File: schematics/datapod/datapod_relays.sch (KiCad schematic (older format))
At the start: 8 parts, among them K1 DS2E-SL2-DC5V, K2 DS2E-SL2-DC5V, Q1 FDG1024NZ, Q2 FDG1024NZ

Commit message: modified schematic
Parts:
- K1, K2: symbol Relays_user_made:DS2E-SL2-DC5V -> datapod-rescue:DS2E-SL2-DC5V-Relays_user_made
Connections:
- net +5V: now also K1.~, K2.~
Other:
- note added: "APPLIES +14.8V TO WIRE/PIN #3\nOF THE LPBH-MP CONNECTOR.\n\nWIRE/PIN #4 SHOULD BE \nCONNECTED TO GND \n\n"
- note added: "THE RELAYS ARE IN A RESET CONDITION WHEN THE\nCOIL ON PINS 2 & 15 IS ACTIVATED. iN A RESET CONDITION\n4 & 6 ARE SHORTED AND 13 &11 ARE SHORTED.\n\nWHEN THE COIL ON PINS 1 & 16 IS ACTIVATED THEN PINS 4 & 8 ARE\nSHORTED AND PINS 13 & 9 ARE SHORTED."
- note added: "THIS REALY WILL BE USED TO\nTURN ON THE RASPBERRY PI\nAND THE IRIDIUM MODEM."
- note added: "THIS RELAY WILL BE USED TO \nENABLE THE BURN WIRE RELEASE"
- moved on the sheet: D1, D2, D3, D4, Q1A, Q1B, Q2A, Q2B

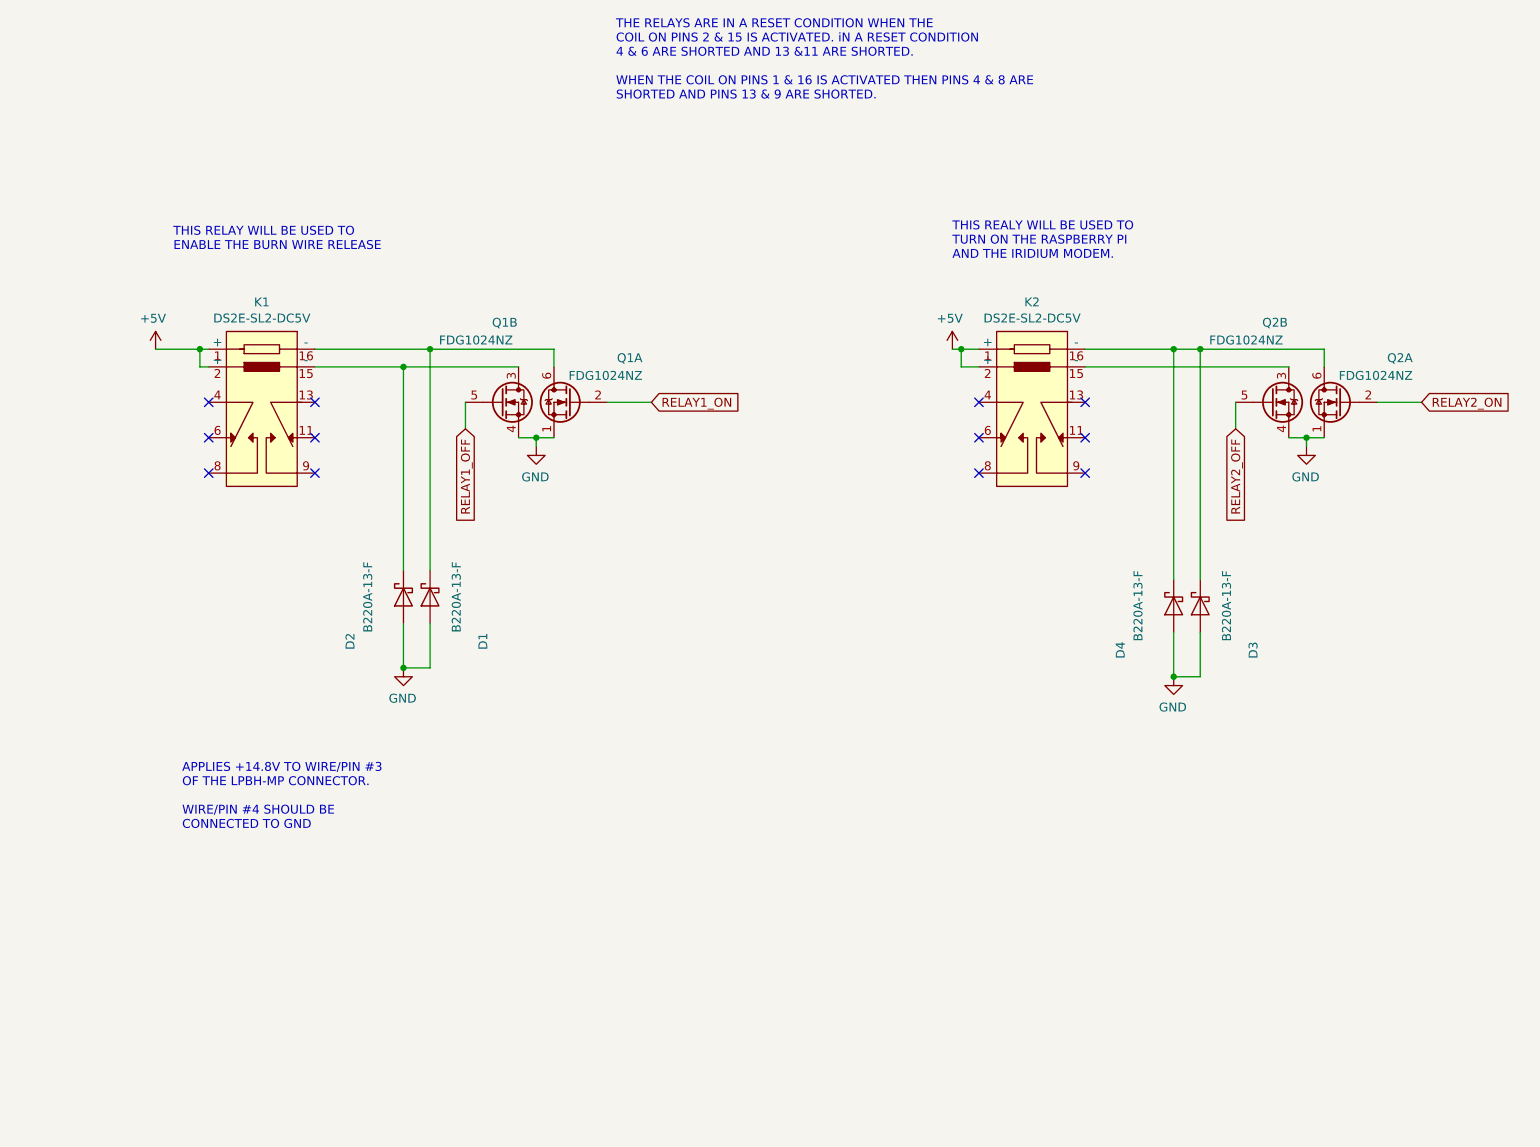
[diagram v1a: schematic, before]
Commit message: added more connectors and started drawing the PCB
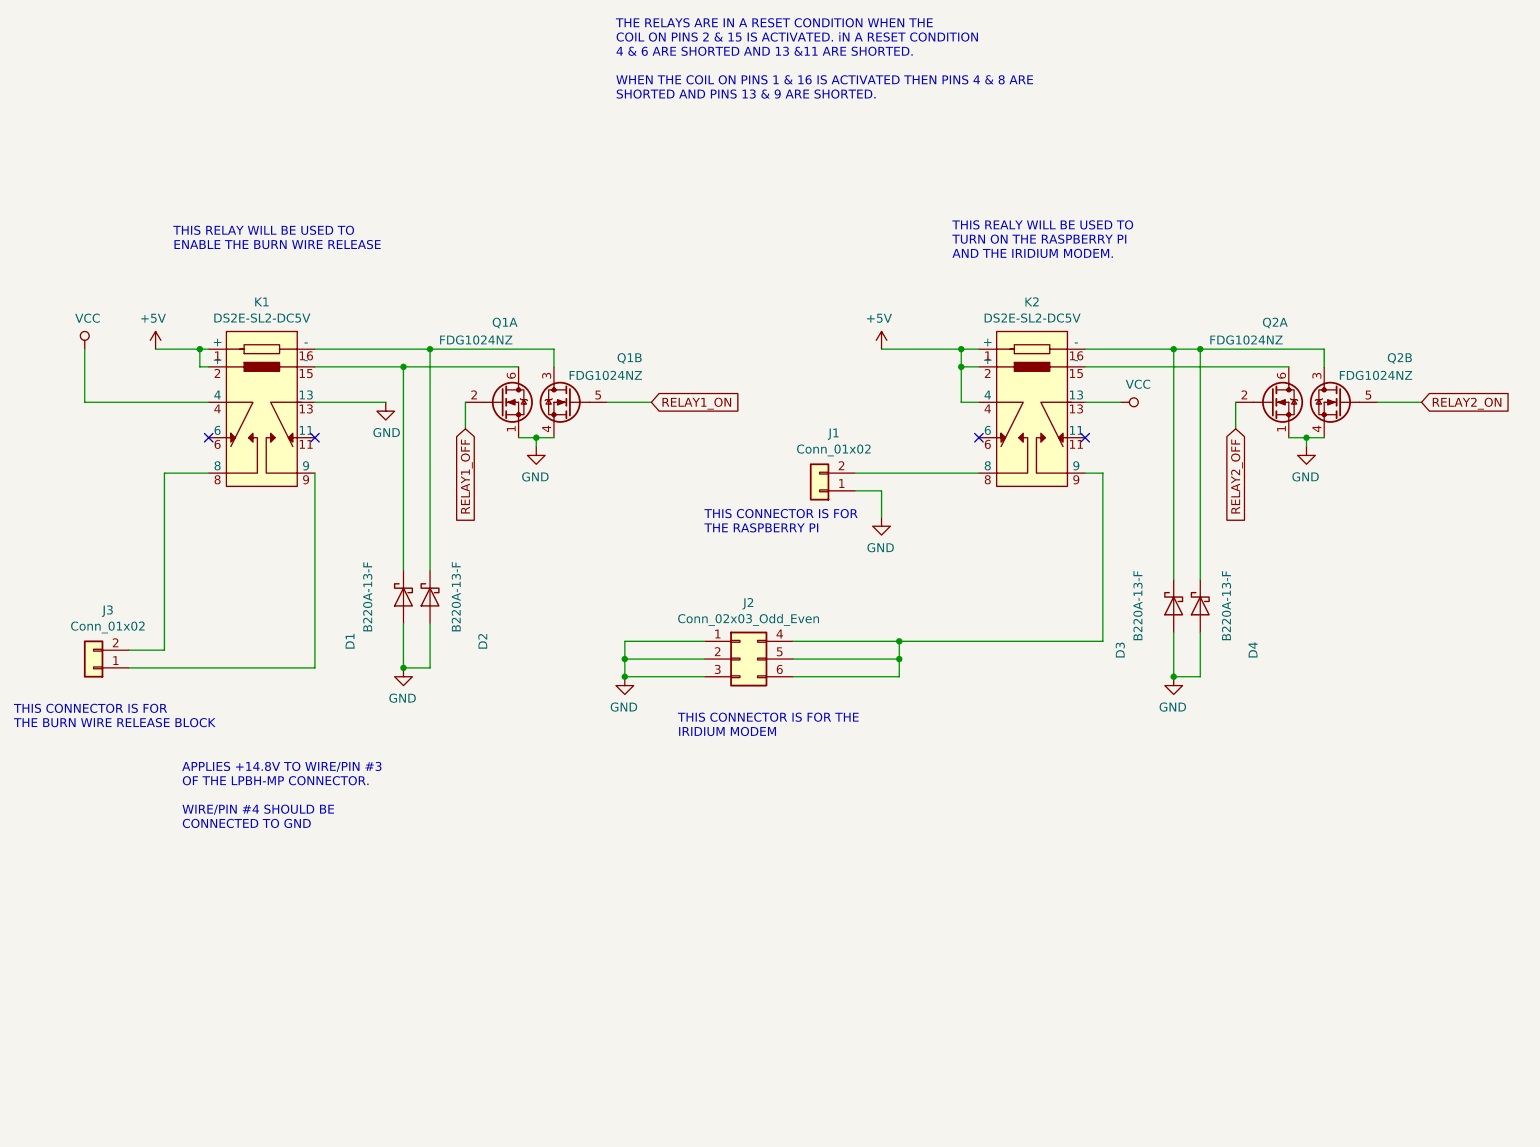
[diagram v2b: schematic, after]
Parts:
- removed K1, K2: DS2E-SL2-DC5V, Package_DIP:DIP-16_W7.62mm_SMDSocket_SmallPads, symbol datapod-rescue:DS2E-SL2-DC5V-Relays_user_made
- added J1: Conn_01x02, Connector_Molex:Molex_Mini-Fit_Jr_5569-02A1_2x01_P4.20mm_Horizontal, symbol Connector_Generic:Conn_01x02
- added J2: Conn_02x03_Odd_Even, Connector_Molex:Molex_Mega-Fit_76825-0006_2x03_P5.70mm_Horizontal, symbol Connector_Generic:Conn_02x03_Top_Bottom
- added J3: Conn_01x02, Connector_Molex:Molex_Mega-Fit_76825-0002_2x01_P5.70mm_Horizontal, symbol Connector_Generic:Conn_01x02
- added K1, K2: DS2E-SL2-DC5V, Package_DIP:DIP-16_W7.62mm_SMDSocket_SmallPads, symbol Relays_user_made:DS2E-SL2-DC5V
- renumbered D2 to D1, D1 to D2, D4 to D3, D3 to D4
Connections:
- net +5V: now also K1.1 (+), K1.2 (+), K2.1 (+), K2.2 (+), K2.4
- net GND: now also Q1.1 (S), Q1.4 (S), Q2.1 (S), Q2.4 (S), J1.1 (Pin_1), J2.1 (Pin_1), J2.2 (Pin_2), J2.3 (Pin_3), K1.13; no longer Q1.1 (S), Q1.4 (S), Q2.1 (S), Q2.4 (S)
- net RELAY1_OFF: now also Q1.2 (G); no longer Q1.5 (G)
- net RELAY1_ON: now also Q1.5 (G); no longer Q1.2 (G)
- net RELAY2_OFF: now also Q2.2 (G); no longer Q2.5 (G)
- net RELAY2_ON: now also Q2.5 (G); no longer Q2.2 (G)
- net at D3.1 (K), D4.1 (K): now also Q2.3 (D), K2.16 (-); no longer Q2.6 (D)
- net at D1.1 (K): now also Q1.6 (D), K1.15 (-); no longer Q1.3 (D)
- net at D2.1 (K): now also Q1.3 (D), K1.16 (-); no longer Q1.6 (D)
- new net: J3.1 (Pin_1), K1.9
- new net: J3.2 (Pin_2), K1.8
- new net: J2.4 (Pin_4), J2.5 (Pin_5), J2.6 (Pin_6), K2.9
- new net: K2.15 (-), Q2.6 (D)
- new net: J1.2 (Pin_2), K2.8
- new net VCC: K1.4, K2.13
- no-connect marks 12 -> 4
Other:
- note added: "THIS CONNECTOR IS FOR THE\nIRIDIUM MODEM"
- note added: "THIS CONNECTOR IS FOR \nTHE RASPBERRY PI"
- note added: "THIS CONNECTOR IS FOR\nTHE BURN WIRE RELEASE BLOCK"

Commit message: added final routed PCB, gerbers and BOM
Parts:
- D1, D2, D3, D4: Part# (none) -> B220A-FDIDKR-ND
- K1, K2: Part# (none) -> 255-1066-ND; Vendor (none) -> Digikey
- Q1, Q2: Part# (none) -> FDG1024NZFSCT-ND; part# FDG1024NZFSCT-ND -> (none)
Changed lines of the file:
@@
 F 3 "http://www.fairchildsemi.com/ds/FD/FDG1024NZ.pdf" H 3900 3000 50  0001 L CNN
 F 4 "Digikey" H 3900 3000 50  0001 C CNN "Vendor"
-F 5 "FDG1024NZFSCT-ND" H 3900 3000 50  0001 C CNN "part#"
+F 5 "FDG1024NZFSCT-ND" H 3900 3000 50  0001 C CNN "Part#"
 	2    3900 3000
 	-1   0    0    -1
@@
 F 3 "http://www.fairchildsemi.com/ds/FD/FDG1024NZ.pdf" H 3500 3000 50  0001 L CNN
 F 4 "Digikey" H 3500 3000 50  0001 C CNN "Vendor"
-F 5 "FDG1024NZFSCT-ND" H 3500 3000 50  0001 C CNN "part#"
+F 5 "FDG1024NZFSCT-ND" H 3500 3000 50  0001 C CNN "Part#"
 	1    3500 3000
 	1    0    0    -1
@@
 F 3 "http://www.jameco.com/Jameco/Products/ProdDS/1538777.pdf" H 2950 4100 50  0001 C CNN
 F 4 "Digikey" H 2950 4100 50  0001 C CNN "Vendor"
+F 5 "B220A-FDIDKR-ND" H 2950 4100 50  0001 C CNN "Part#"
 	1    2950 4100
 	0    -1   1    0
@@
 F 3 "http://www.jameco.com/Jameco/Products/ProdDS/1538777.pdf" H 3100 4100 50  0001 C CNN
 F 4 "Digikey" H 3100 4100 50  0001 C CNN "Vendor"
+F 5 "B220A-FDIDKR-ND" H 3100 4100 50  0001 C CNN "Part#"
 	1    3100 4100
 	0    -1   1    0
@@
 F 3 "http://www.fairchildsemi.com/ds/FD/FDG1024NZ.pdf" H 7850 3000 50  0001 L CNN
 F 4 "Digikey" H 7850 3000 50  0001 C CNN "Vendor"
-F 5 "FDG1024NZFSCT-ND" H 7850 3000 50  0001 C CNN "part#"
+F 5 "FDG1024NZFSCT-ND" H 7850 3000 50  0001 C CNN "Part#"
 	1    7850 3000
 	1    0    0    -1
@@
 F 3 "http://www.fairchildsemi.com/ds/FD/FDG1024NZ.pdf" H 8250 3000 50  0001 L CNN
 F 4 "Digikey" H 8250 3000 50  0001 C CNN "Vendor"
-F 5 "FDG1024NZFSCT-ND" H 8250 3000 50  0001 C CNN "part#"
+F 5 "FDG1024NZFSCT-ND" H 8250 3000 50  0001 C CNN "Part#"
 	2    8250 3000
 	-1   0    0    -1
@@
 F 3 "http://www.jameco.com/Jameco/Products/ProdDS/1538777.pdf" H 7300 4150 50  0001 C CNN
 F 4 "Digikey" H 7300 4150 50  0001 C CNN "Vendor"
+F 5 "B220A-FDIDKR-ND" H 7300 4150 50  0001 C CNN "Part#"
 	1    7300 4150
 	0    -1   1    0
@@
 F 3 "http://www.jameco.com/Jameco/Products/ProdDS/1538777.pdf" H 7450 4150 50  0001 C CNN
 F 4 "Digikey" H 7450 4150 50  0001 C CNN "Vendor"
+F 5 "B220A-FDIDKR-ND" H 7450 4150 50  0001 C CNN "Part#"
 	1    7450 4150
 	0    -1   1    0
@@
 F 2 "Package_DIP:DIP-16_W7.62mm_SMDSocket_SmallPads" H 6550 2500 50  0001 C CNN
 F 3 "https://www3.panasonic.biz/ac/e_download/control/relay/signal/catalog/mech_eng_ds.pdf" H 6550 2500 50  0001 C CNN
+F 4 "Digikey" H 6550 2450 50  0001 C CNN "Vendor"
+F 5 "ED11092-ND" H 6550 2450 50  0001 C CNN "Part#"
+F 6 "255-1066-ND" H 6550 2450 50  0001 C CNN "Part#"
 	1    6550 2450
 	1    0    0    -1
@@
 F 2 "Package_DIP:DIP-16_W7.62mm_SMDSocket_SmallPads" H 2200 2500 50  0001 C CNN
 F 3 "https://www3.panasonic.biz/ac/e_download/control/relay/signal/catalog/mech_eng_ds.pdf" H 2200 2500 50  0001 C CNN
+F 4 "Digikey" H 2200 2450 50  0001 C CNN "Vendor"
+F 5 "ED11092-ND" H 2200 2450 50  0001 C CNN "Part#"
+F 6 "255-1066-ND" H 2200 2450 50  0001 C CNN "Part#"
 	1    2200 2450
 	1    0    0    -1
